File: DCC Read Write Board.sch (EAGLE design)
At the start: 60 parts, among them IC5 4163D, K1 68613014122, K2 686318124422, Q181 744053D, Q182 74HCT175D, Q183 74HC00D, U185 74HC02D

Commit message: Most of the Write amp and logic gate schematic done
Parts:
- removed C10, C5: 100nF, rcl:C-EUC0603
- removed K2: 686318124422, FPC_Connectors_Flat_Flexible_Cable_rev15c:686318124422
- removed U$1: TDA1317, dcc:TDA1317
- removed U$2: TDA1316, dcc:TDA1316
- added C133, C134, C138, C151, C152, C181, C183, C185: 100nF, rcl:C-EUC0603
- added C135, C137, C148, C150: 68uF 10V, rcl:CPOL-EU153CLV-0405
- added J103: 686318124422, FPC_Connectors_Flat_Flexible_Cable_rev15c:686318124422
- added Q1: MUN2211T1, transistor-npn:MUN2211T1
- added Q101: TDA1317, dcc:TDA1317
- added Q102, Q103, Q180: 2SC2712GR, transistor-npn:BC849SMD
- added Q104: 2SD99CL, transistor-npn:BC849SMD
- added Q151: TDA1316, dcc:TDA1316
- added R1, R2: 560R, rcl:R-EU_R0603
- added R151: 12R, rcl:R-EU_R0603
- added R155: 2K2, rcl:R-EU_R0603
- added R156: 220R, rcl:R-EU_R0603
- added R167: 100R, pot-vitrohm:PC25
- added R180: 1K, rcl:R-EU_R0603
- added R181: 330R, rcl:R-EU_R0603
- added R182: 10R, rcl:R-EU_R0603
- added R183: 12K, rcl:R-EU_R0603
- added R184: 47R, rcl:R-EU_R0603
- added R185: 1K8, rcl:R-EU_R0603
- added R186: 68R, rcl:R-EU_R0603
- added R187: (no value), ptc-ntc:NTC640
- C2, C3: value 100nF -> 1uF
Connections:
- new net +8V: C133.1, C148.+, J103.14, Q102.C, Q103.C, Q104.C, R1.2
- new net 1: J103.1
- new net 10: J103.10
- new net 12: J103.12
- new net 3: J103.3
- new net 4: J103.4
- new net 5: J103.5
- new net 6: J103.6
- new net 8: J103.8
- new net ANA_L: J103.18
- new net ANA_R: J103.16
- new net CC/!DCC: J103.13, Q1.B
- new net N$11: IC5G$1.!LOAD, Q181G$1.S2, Q183C.O
- new net N$12: Q181G$1.3Y0, Q182A.Q1, Q183C.I1
- new net N$13: IC5G$1.CO, Q181G$1.S1, Q182A.D4, Q183A.I1, U185B.I0
- new net N$14: Q181G$1.2Z, Q182A.D2
- new net N$15: Q181G$1.S3, Q183A.O
- new net N$16: Q182A.!Q2, Q183A.I0
- new net N$17: Q182A.Q4, U185B.I1
- new net N$18: U185B.O, U185C.I1, U185D.I0
- new net N$28: Q181G$1.3Y1, Q182A.Q3, U185A.I1
- new net N$29: Q181G$1.1Z, Q181G$1.2Y1
- new net N$39: Q181G$1.1Y0, Q182A.Q2, U185A.I0
- new net N$40: U185A.O, U185C.I0
- new net N$41: Q182A.!Q3, U185D.I1
- new net N$42: Q181G$1.3Z, Q182A.D3
- new net N$43: R183.1, U185C.O
- new net N$44: Q1.C, Q101.REF2@9
- new net N$45: R180.1, U185D.O
- new net N$46: Q180.B, R180.2, R181.2
- new net N$47: Q180.E, R182.2
- new net N$48: Q151.SENSE_R@11, R156.2, R167.E, R167.S
- new net N$49: Q151.IWR_R@12, R155.2, R167.A
- new net N$50: Q151.CLAMP@8, R151.2
- new net N$51: Q102.E, Q103.B, Q104.B
- new net N$52: C137.+, C138.1, Q102.B, R1.1, R2.2
- new net R184_END: R184.1, R185.1, R186.2, R187.1
- new net RD_LCK: J103.9
- new net RD_MUX: J103.7
- new net RD_SYNK: J103.11
- new net SENSE_GND: Q151.SENSE_GND@9, R183.2, R184.2
- new net SOURCE: Q151.SOURCE@6, Q180.C
- new net VSENSE_2: C3.1, Q103.E
- net +5V: now also C134.1, C135.+, C150.+, C151.1, C152.2, C181.1, C183.1, C185.1, IC5G$1.!CLEAR, J103.15, Q101.VCCA@21, Q101.VCCM@36, Q101.VDD@4, Q151.ANA_VDD@10, Q151.DIG_VDD@4, Q151.VDD@19, Q181G$1.1Y1, Q182A.CLR, R151.1, R185.2; no longer C10.2, C2.1, C3.1, C5.1, U$1.VCCA@21, U$1.VCCM@36, U$1.VDD@4, U$2.VDD@19
- net GND: now also C133.2, C134.2, C135.-, C137.-, C138.2, C148.-, C150.-, C151.2, C152.1, C181.2, C183.2, C185.2, J103.17, J103.2, Q1.E, Q101.VEEA@28, Q101.VEED@16, Q101.VEEM@29, Q101.VSS@8, Q151.ANA_GND@13, Q151.DIG_GND@3, Q181G$1.2Y0, Q181G$1.E, Q183B.I0, Q183B.I1, R155.1, R156.1, R181.1, R182.1, R186.1, R187.2, R2.1; no longer C10.1, C5.2, U$1.VEEA@28, U$1.VEED@16, U$1.VEEM@29, U$1.VSS@8, U$2.ANA_GND@13
- net IRH0: now also Q151.QA@24; no longer U$2.QA@24
- net IRH1: now also Q151.QB@23; no longer U$2.QB@23
- net IRH2: now also Q151.QC@22; no longer U$2.QC@22
- net IRH3: now also Q151.QD@21; no longer U$2.QD@21
- net IRH4: now also Q151.QE@20; no longer U$2.QE@20
- net IRH5: now also Q151.QF@18; no longer U$2.QF@18
- net IRH6: now also Q151.QG@17; no longer U$2.QG@17
- net IRH7: now also Q151.QH@16; no longer U$2.QH@16
- net IRH8: now also Q151.QI@15; no longer U$2.QI@15
- net IRH9: now also Q151.QJ@14; no longer U$2.QJ@14
- net N$1: now also Q101.IN7@20; no longer U$1.IN7@20
- net N$2: now also Q101.IN6@19; no longer U$1.IN6@19
- net N$3: now also Q101.IN5@18; no longer U$1.IN5@18
- net N$4: now also Q101.IN4@17; no longer U$1.IN4@17
- net N$5: now also Q101.IN3@15; no longer U$1.IN3@15
- net N$6: now also Q101.IN2@14; no longer U$1.IN2@14
- net N$7: now also Q101.IN1@13; no longer U$1.IN1@13
- net N$8: now also Q101.IN0@12; no longer U$1.IN0@12
- net N$9: now also Q101.INAUX@11; no longer U$1.INAUX@11
- net VSENSE_1: now also C2.1, Q104.E
- net WCLOCK: now also Q151.WCLOCK@1; no longer U$2.WCLOCK@1
- net WDATA: now also Q151.WDATA@2; no longer U$2.WDATA@2
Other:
- note added: "IREC ADJ"
- note added: "nc"

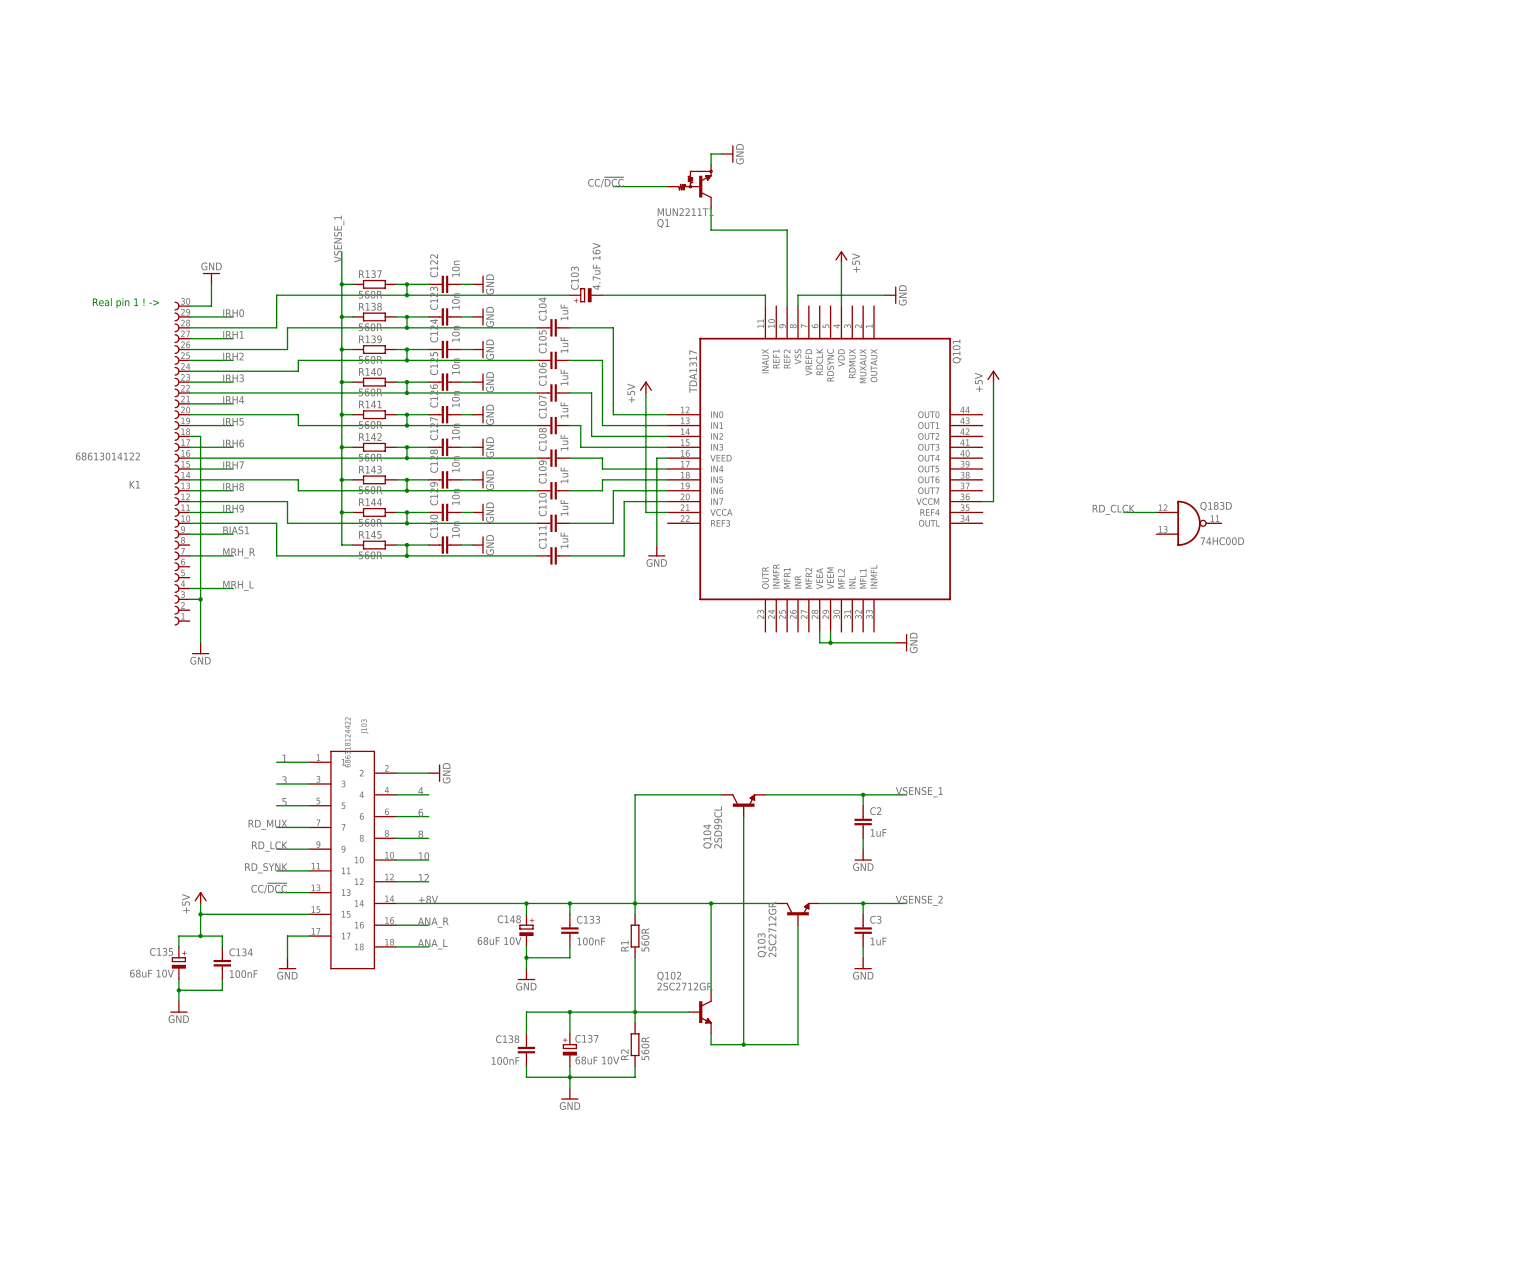
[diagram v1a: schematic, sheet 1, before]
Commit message: Everything added to schematic, but needs checking
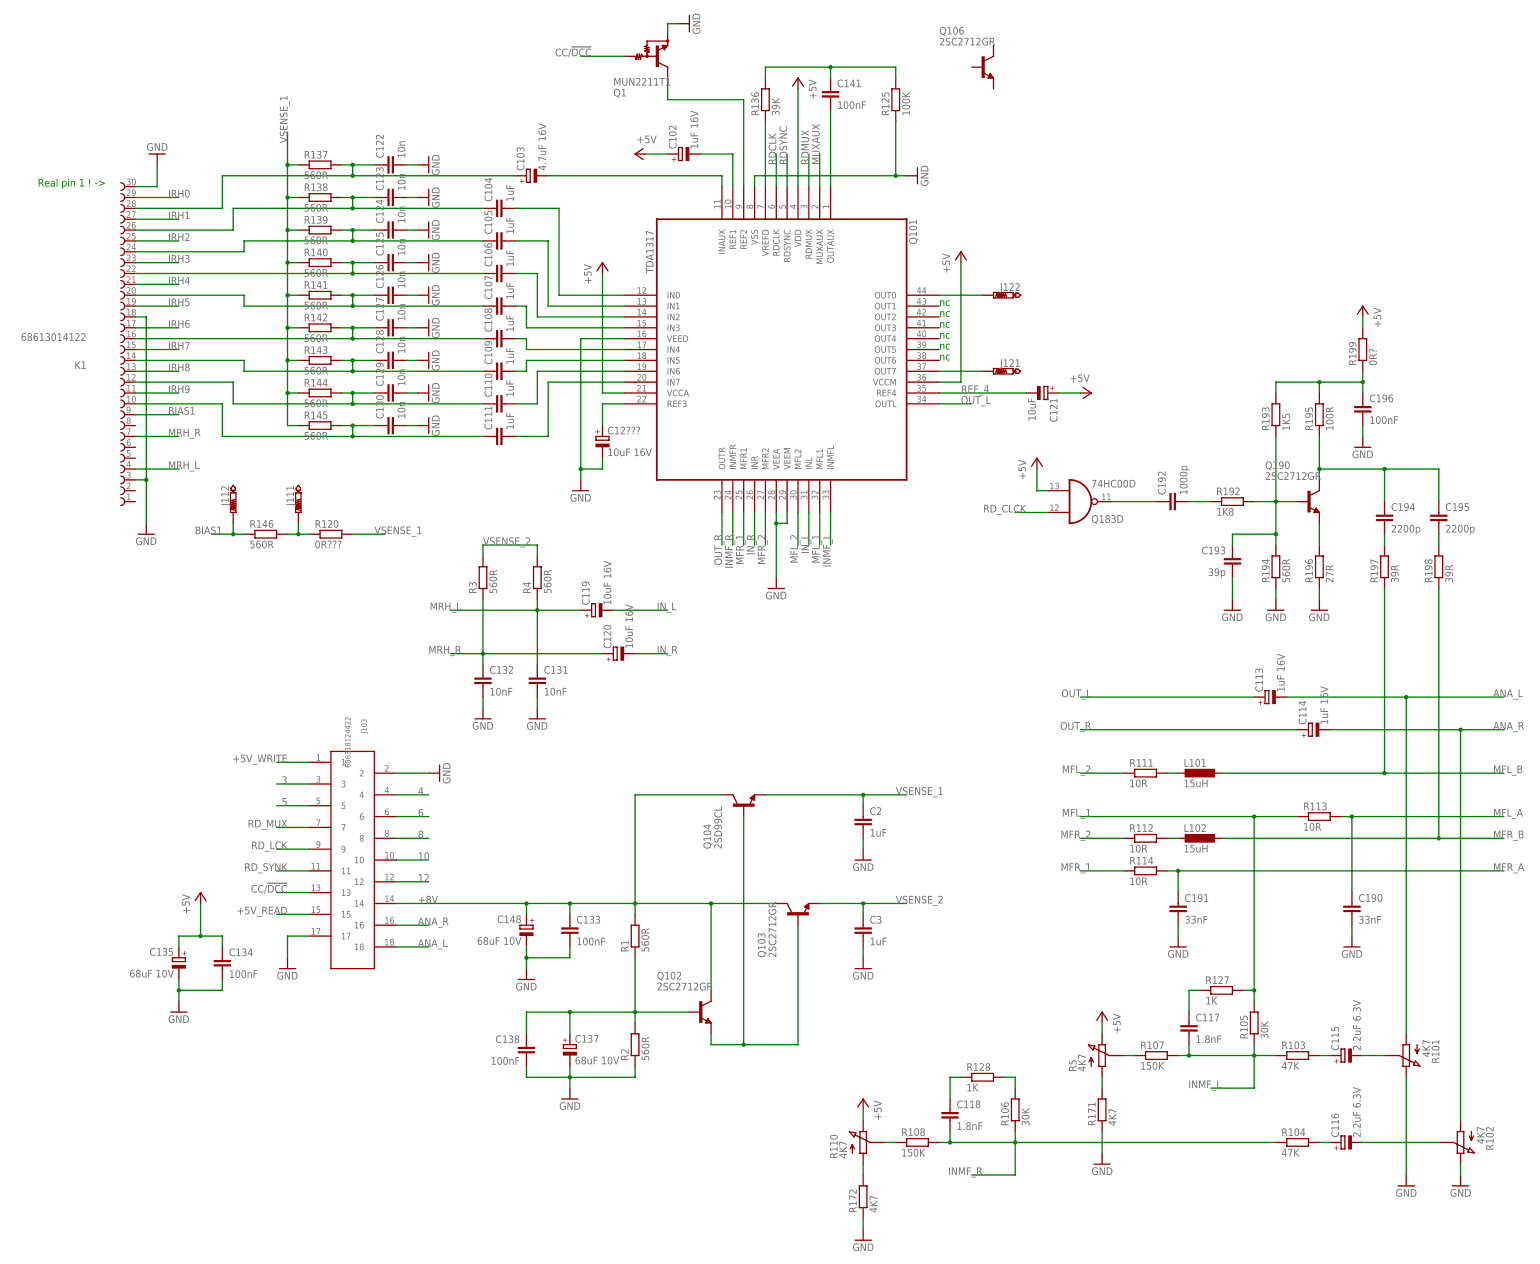
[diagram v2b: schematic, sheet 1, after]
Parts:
- added C102, C113, C114: 1uF 16V, rcl:CPOL-EU153CLV-0505
- added C115, C116: 2.2uF 6.3V, rcl:CPOL-EU153CLV-0505
- added C117, C118: 1.8nF, rcl:C-EUC0603
- added C119, C120, C12???: 10uF 16V, rcl:CPOL-EU153CLV-0505
- added C121: 10uF, rcl:CPOL-EU153CLV-0505
- added C131, C132: 10nF, rcl:C-EUC0603
- added C141, C196: 100nF, rcl:C-EUC0603
- added C190, C191: 33nF, rcl:C-EUC0603
- added C192: 1000p, rcl:C-EUC0603
- added C193: 39p, rcl:C-EUC0603
- added C194, C195: 2200p, rcl:C-EUC0603
- added J111, J112, J121, J122: PTR1PAD1-17, testpad:PTR1PAD1-17
- added L101, L102: 15uH, rcl:L-EUL1812
- added Q106, Q190: 2SC2712GR, transistor-npn:BC849SMD
- added R101, R102, R110, R5: 4K7, pot-vitrohm:PC25
- added R103, R104: 47K, rcl:R-EU_R0603
- added R105, R106: 30K, rcl:R-EU_R0603
- added R107, R108: 150K, rcl:R-EU_R0603
- added R111, R112, R113, R114: 10R, rcl:R-EU_R0603
- added R120: 0R???, rcl:R-EU_R0603
- added R125: 100K, rcl:R-EU_R0603
- added R127, R128: 1K, rcl:R-EU_R0603
- added R136: 39K, rcl:R-EU_R0603
- added R146, R194, R3, R4: 560R, rcl:R-EU_R0603
- added R171, R172: 4K7, rcl:R-EU_R0603
- added R192: 1K8, rcl:R-EU_R0603
- added R193: 1K5, rcl:R-EU_R0603
- added R195: 100R, rcl:R-EU_R0603
- added R196: 27R, rcl:R-EU_R0603
- added R197, R198: 39R, rcl:R-EU_R0603
- added R199: 0R?, rcl:R-EU_R0603
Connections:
- net 1 renamed +5V_WRITE
- new net +5V_READ: J103.15
- new net INMF_L: C117.2, Q101.INMFL@33, R103.1, R105.1, R107.2
- new net INMF_R: C118.2, Q101.INMFR@24, R104.1, R106.1, R108.2
- new net IN_L: C119.-, Q101.INL@31
- new net IN_R: C120.-, Q101.INR@26
- new net MFL_1: Q101.MFL1@32, R105.2, R113.1, R127.2
- new net MFL_2: Q101.MFL2@30, R111.1
- new net MFL_3: R106.2, R128.2
- new net MFL_A: C190.1, R113.2
- new net MFL_B: L101.1, R197.1
- new net MFR_1: Q101.MFR1@25, R114.1
- new net MFR_2: Q101.MFR2@27, R112.1
- new net MFR_A: C191.1, R114.2
- new net MFR_B: L102.1, R198.1
- new net MUXAUX: Q101.MUXAUX@2
- new net N$53: C102.-, Q101.REF1@10
- new net N$54: C141.2, Q101.OUTAUX@1
- new net N$55: Q101.VREFD@7, R136.1
- new net N$56: C141.1, R125.2, R136.2
- new net N$57: C12???.+, Q101.REF3@22
- new net N$58: C192.1, Q183D.O
- new net N$59: C192.2, R192.1
- new net N$60: C196.1, R193.2, R195.2, R199.1
- new net N$61: C193.1, Q190.B, R192.2, R193.1, R194.2
- new net N$62: C194.1, C195.1, Q190.C, R195.1
- new net N$63: Q190.E, R196.2
- new net N$64: C195.2, R198.2
- new net N$65: C194.2, R197.2
- new net N$66: L102.2, R112.2
- new net N$67: L101.2, R111.2
- new net N$68: J122.TP, Q101.OUT0@44
- new net N$69: J121.TP, Q101.OUT7@37
- new net N$70: J111.TP, R120.1, R146.2
- new net N$71: C115.-, R101.S
- new net N$72: C116.-, R102.S
- new net N$73: C115.+, R103.2
- new net N$74: C116.+, R104.2
- new net N$76: C117.1, R127.1
- new net N$77: R107.1, R5.S
- new net N$79: C118.1, R128.1
- new net N$80: R108.1, R110.S
- new net N$81: R171.2, R5.A
- new net N$82: R110.A, R172.2
- new net OUT_L: C113.+, Q101.OUTL@34
- new net OUT_R: C114.+, Q101.OUTR@23
- new net RDCLK: Q101.RDCLK@6
- new net RDMUX: Q101.RDMUX@3
- new net RDSYNC: Q101.RDSYNC@5
- new net REF_4: C121.-, Q101.REF4@35
- net +5V: now also C102.+, C121.+, Q183D.I1, R110.E, R199.2, R5.E; no longer J103.15
- net ANA_L: now also C113.-, R101.A
- net ANA_R: now also C114.-, R102.A
- net BIAS1: now also J112.TP, R146.1
- net GND: now also C12???.-, C131.2, C132.2, C190.2, C191.2, C193.2, C196.2, R101.E, R102.E, R125.1, R171.1, R172.1, R194.1, R196.1
- net MRH_L: now also C119.+, C131.1, R4.1
- net MRH_R: now also C120.+, C132.1, R3.1
- net VSENSE_1: now also R120.2
- net VSENSE_2: now also R3.2, R4.2
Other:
- moved on the sheet: C103, C104, C105, C106, C107, C108, C109, C110, C111, C122, C123, C124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

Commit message: Schematic complete. Still needs checking
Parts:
- added C143: 4.7uF 16V, rcl:CPOL-EU153CLV-0505
- added Q2: BCX71SMD, transistor-pnp:BCX71SMD
- added R129: 47R, rcl:R-EU_R0603
- added R130: 470R, rcl:R-EU_R0603
- added R131: 330R, rcl:R-EU_R0603
- added R132: 560R, rcl:R-EU_R0603
- added R133: 8K2, rcl:R-EU_R0603
- added R134: 12K, rcl:R-EU_R0603
- added R135: 1K, pot-vitrohm:PC25
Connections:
- removed net +5V: C1.1, C102.+, C121.+, C134.1, C135.+, C150.+, C151.1, C152.2, C181.1, C183.1, C185.1, C4.1, IC5G$1.!CLEAR, IC5G$1.P1, IC5G$1.P4, IC5G$1.PE, IC5G$1.TE, IC5P.VDD, Q101.VCCA@21, Q101.VCCM@36, Q101.VDD@4, Q151.ANA_VDD@10, Q151.DIG_VDD@4, Q151.VDD@19, Q181G$1.1Y1, Q181P.VCC, Q182A.CLR, Q182P.VCC, Q183D.I1, Q183P.VCC, R110.E, R151.1, R185.2, R199.2, R5.E, U185P.VCC
- removed net 10: J103.10
- removed net 12: J103.12
- removed net 3: J103.3
- removed net 4: J103.4
- removed net 5: J103.5
- removed net 6: J103.6
- removed net 8: J103.8
- removed net RDCLK: Q101.RDCLK@6
- removed net RDSYNC: Q101.RDSYNC@5
- removed net RD_LCK: J103.9
- removed net RD_SYNK: J103.11
- removed net WCLOCK: IC5G$1.CLK, Q151.WCLOCK@1, Q182A.CLK
- new net N$75: C143.-, Q106.B, R133.2, R134.1
- new net N$78: Q106.E, R130.1, R131.2
- new net N$83: Q106.C, Q2.B, R132.1
- new net N$84: Q2.C, R129.1, R130.2
- new net N$85: C143.+, R135.S
- new net RD_SYNC: J103.11, Q101.RDSYNC@5
- new net WCLCK: IC5G$1.CLK, J103.3, Q151.WCLOCK@1, Q182A.CLK
- net +5V_READ: now also C102.+, C121.+, C134.1, C135.+, Q101.VCCA@21, Q101.VCCM@36, Q101.VDD@4, Q2.E, R110.E, R132.2, R134.2, R199.2, R5.E
- net +5V_WRITE: now also C1.1, C150.+, C151.1, C152.2, C181.1, C183.1, C185.1, C4.1, IC5G$1.!CLEAR, IC5G$1.P1, IC5G$1.P4, IC5G$1.PE, IC5G$1.TE, IC5P.VDD, Q151.ANA_VDD@10, Q151.DIG_VDD@4, Q151.VDD@19, Q181G$1.1Y1, Q181P.VCC, Q182A.CLR, Q182P.VCC, Q183D.I1, Q183P.VCC, R151.1, R185.2, U185P.VCC
- net GND: now also J103.10, J103.12, J103.4, J103.6, J103.8, R131.1, R133.1, R135.A
- net RDMUX: now also R135.E
- net RD_CLCK: now also J103.9, Q101.RDCLK@6
- net RD_MUX: now also R129.2
- net WDATA: now also J103.5
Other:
- moved on the sheet: C1, C115, C116, C134, C135, C141, C150, C151, C152, C157, C158, C159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
